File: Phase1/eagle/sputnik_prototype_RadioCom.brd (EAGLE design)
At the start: 99 x 100 mm, 103 parts, among them Y1 32MHz

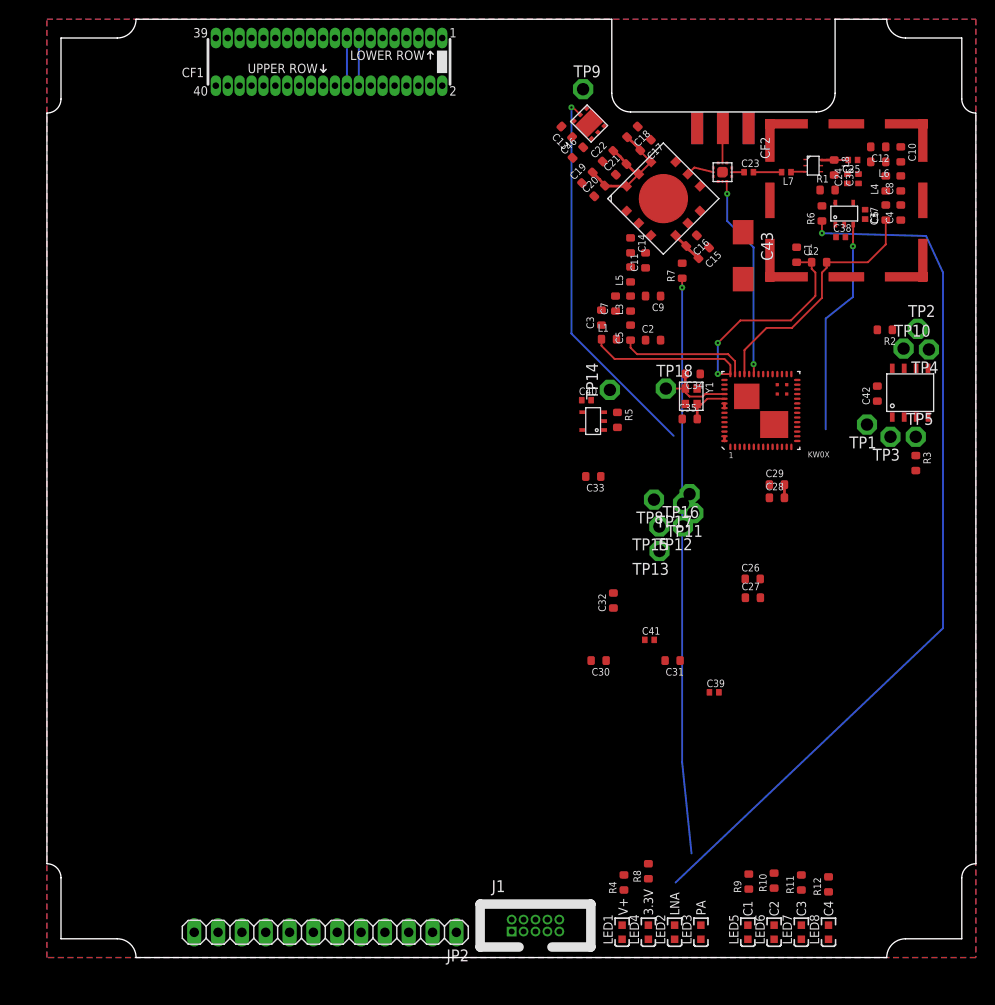
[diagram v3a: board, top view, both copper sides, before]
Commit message: Yep, that was a good idea. I added the other shield. And experimented with other layouts. Still needs a ton of work, but now it's going to be OK. OH CRAP the RXTX switch might have be wired the otherway: check this. That said, I think this is more sane. Power and nd caps need to be laid out, then signals.
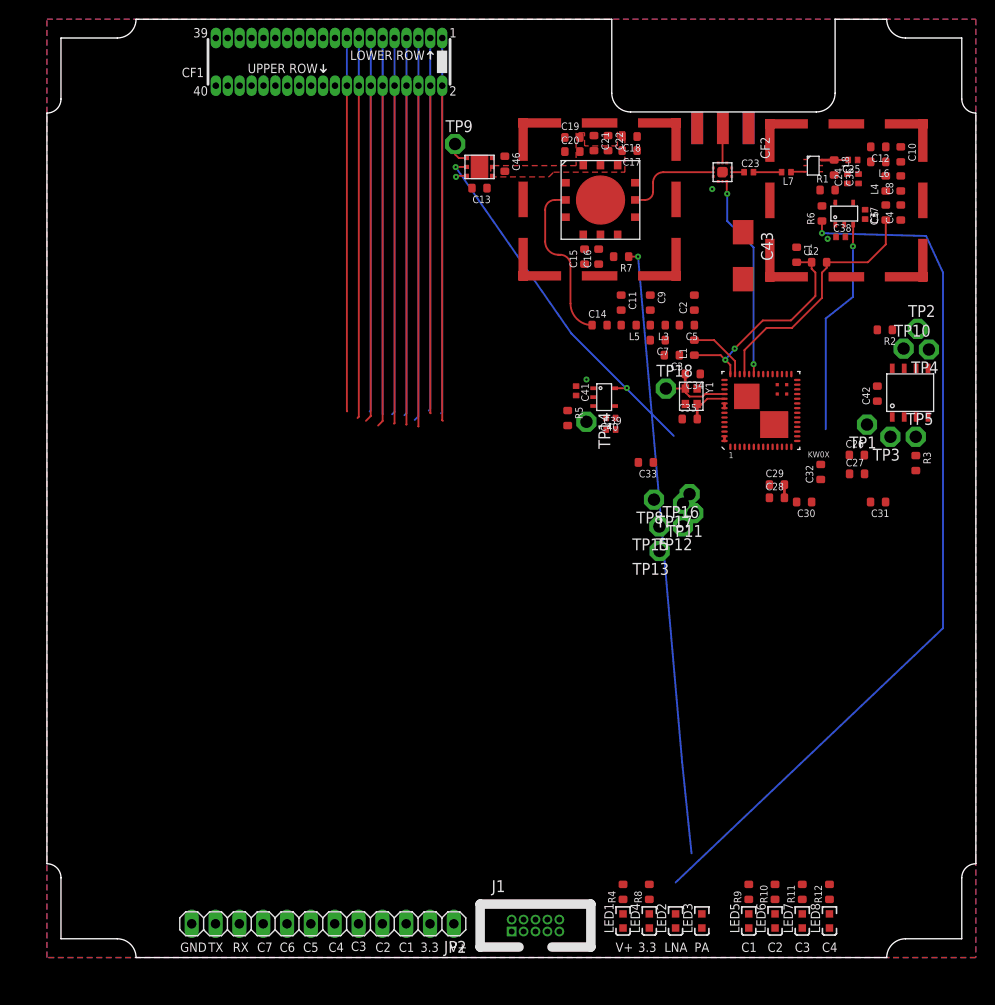
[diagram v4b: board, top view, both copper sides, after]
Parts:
- added SH2: BMI-S-202-SHIELD, hw-laird-bmi-s-202:BMI-S-202
- moved C39 30.1 mm to (60.1, 56.3)
- moved C41 27.7 mm to (56.4, 60.4), turned to 270 degrees
- moved C30 27.7 mm to (80.7, 48.5)
- moved C31 27.7 mm to (88.6, 48.5)
- moved C32 26.0 mm to (82.5, 51.8)
- moved C27 17.2 mm to (86.3, 51.5)
- moved C26 17.2 mm to (86.3, 53.5)
- moved TP9 14.8 mm to (43.5, 86.7)
- moved U$9 12.8 mm to (44.6, 83.0), turned to 90 degrees
- moved C15 12.7 mm to (57.3, 74.7), turned to 90 degrees
- moved C13 11.1 mm to (46.1, 82.0), turned to 180 degrees
- moved C16 10.0 mm to (58.8, 74.7), turned to 90 degrees
- moved L1 9.14 mm to (69.0, 65.0), turned to 90 degrees
- moved C14 9.12 mm to (58.9, 67.4), turned to 0 degrees
- moved C3 8.50 mm to (66.6, 64.2), turned to 180 degrees
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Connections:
- net V+ renamed RIP
- net GND: now also SH2.P$1, SH2.P$10, SH2.P$11, SH2.P$12, SH2.P$2, SH2.P$3, SH2.P$4, SH2.P$5, SH2.P$6, SH2.P$7, SH2.P$8, SH2.P$9
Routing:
- net PTC3: track 0.00 -> 40.9 mm
- net PTC5: track 0.00 -> 40.3 mm
- net PTC7: track 0.00 -> 40.2 mm
- net PTE16: track 0.00 -> 40.1 mm
- net PTB2: track 0.00 -> 40.1 mm
- net PTE18: track 0.00 -> 39.8 mm
- net PTC1: track 0.00 -> 39.8 mm
- net PTE17: track 0.00 -> 36.4 mm
- net PTC4: track 0.00 -> 36.3 mm
- net PTC6: track 0.00 -> 36.1 mm
- net PTD0: track 0.00 -> 36.0 mm
- net PTE19: track 0.00 -> 35.9 mm
- net PTB17: track 0.00 -> 35.7 mm
- net UART0_TX: track 5.08 -> 40.6 mm
- net PTC2: track 0.00 -> 34.9 mm
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- added copper zone on layer 15, net 3.3V
- added copper zone on layer 15, net RIP
- added copper zone on layer 1, net VPA
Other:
- board text added: "3.3"
- board text added: "C5"
- board text added: "C6"
- board text added: "C7"
- board text added: "GND"
- board text added: "RX"
- board text added: "TX"
- board text removed: "3.3V"

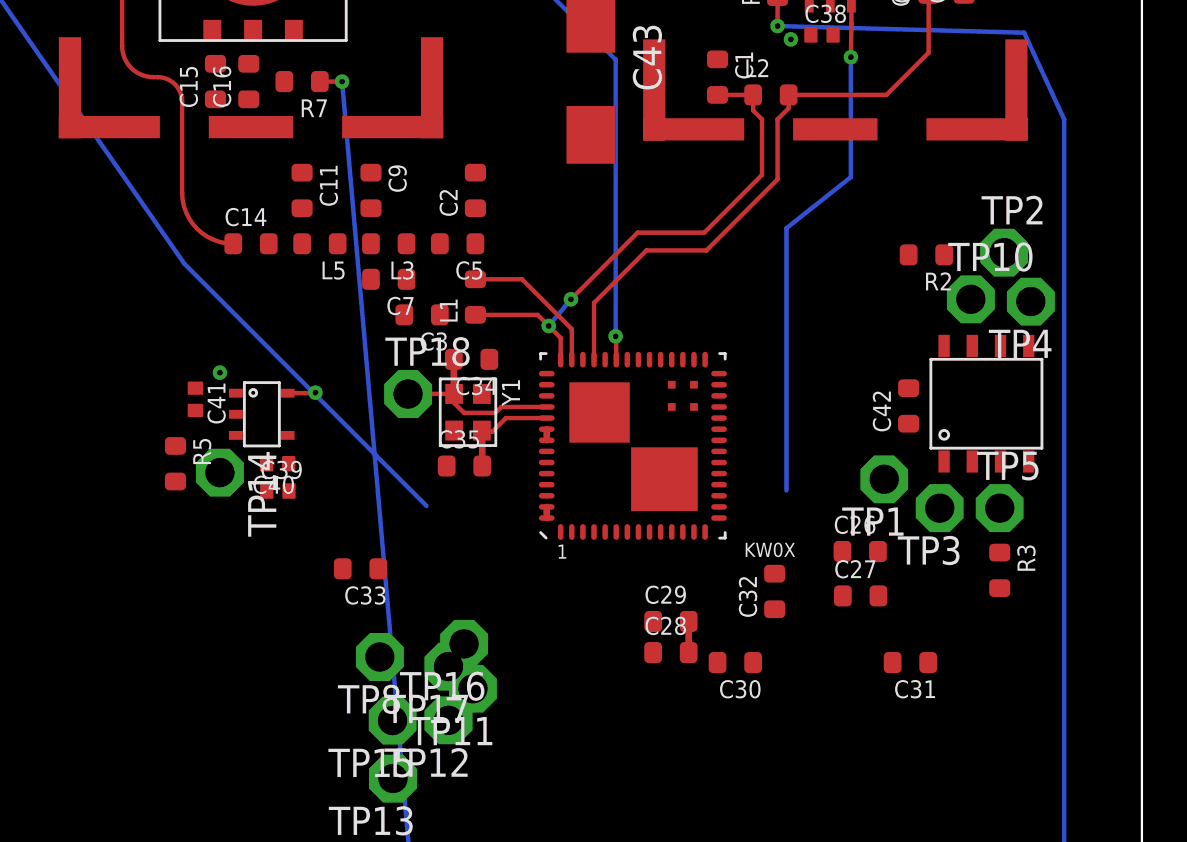
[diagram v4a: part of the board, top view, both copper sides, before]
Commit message: Attached bypass caps, made some connections between LDO and SPI cache components
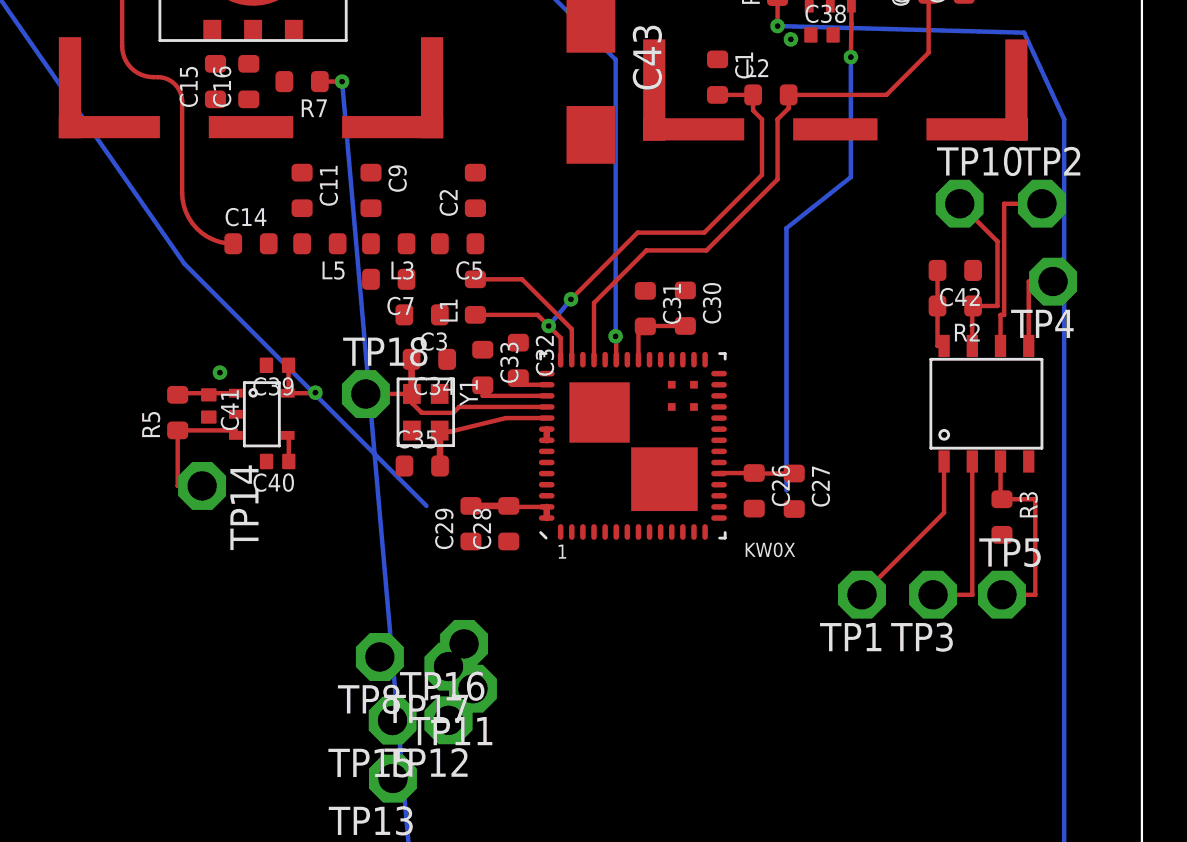
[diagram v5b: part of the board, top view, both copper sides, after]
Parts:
- moved C31 19.9 mm to (76.7, 64.5), turned to 270 degrees
- moved C30 16.1 mm to (78.5, 64.5), turned to 270 degrees
- moved C32 15.5 mm to (70.9, 62.1), turned to 270 degrees
- moved C33 10.6 mm to (69.3, 61.8), turned to 270 degrees
- moved C29 10.0 mm to (68.8, 54.8), turned to 90 degrees
- moved C28 9.32 mm to (70.5, 54.8), turned to 90 degrees
- moved C42 6.45 mm to (90.6, 66.2), turned to 180 degrees
- moved C39 5.66 mm to (60.1, 61.9), turned to 180 degrees
- moved C27 5.58 mm to (83.3, 56.3), turned to 270 degrees
- moved C26 5.50 mm to (81.5, 56.3), turned to 270 degrees
- moved TP1 5.30 mm to (86.4, 51.6)
- moved TP10 4.33 mm to (90.8, 69.2)
- moved TP3 3.91 mm to (89.6, 51.6)
- moved TP5 3.90 mm to (92.7, 51.6)
- moved TP2 2.78 mm to (94.5, 69.2)
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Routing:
- net 3.3V: track 3.16 -> 17.3 mm
- net N$11: track 0.00 -> 9.06 mm
- net SCLK: track 0.00 -> 8.27 mm
- net !HOLD: track 0.00 -> 8.24 mm
- net MISO: track 0.00 -> 7.77 mm
- net !CS: track 0.00 -> 7.53 mm
- net N$12: track 0.00 -> 6.45 mm
- net MOSI: track 0.00 -> 4.00 mm
- net N$34: track 0.00 -> 3.36 mm
- net RIP: track 1.32 -> 4.09 mm
- net N$6: track 8.50 -> 10.4 mm
- net N$8: track 4.80 -> 6.52 mm
- net N$31: track 0.00 -> 1.58 mm
- net N$13: track 0.00 -> 1.23 mm

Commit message: Fixed symbol pins and locations
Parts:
- removed L7: (no value), rcl_custom:.0402-B-NOSILK
- added C44: 10nF, rcl_custom:.0402-B-NOSILK
- C24: value 10nF -> 1nF
- L8: value 150nH -> 82nH
- moved PA 5.80 mm to (58.9, 80.8)
- moved U$1 3.61 mm to (92.0, 59.6)
- moved U$7 1.68 mm to (84.8, 79.0)
- moved TRSWITCH 1.41 mm to (72.0, 83.7)
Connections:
- removed net N$24: L7.1, LNA.3
- net GND: now also C44.2
- net LNA_IN: now also TRSWITCH.8; no longer TRSWITCH.2
- net N$2: now also TRSWITCH.2; no longer TRSWITCH.8
- net N$25: now also LNA.3; no longer L7.2
- net VBIAS: now also C44.1
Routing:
- net 3.3V: track 17.3 -> 20.6 mm
- net N$25: track 3.00 -> 0.00 mm
- net N$2: track 10.1 -> 12.3 mm
- net LNA_IN: track 1.32 -> 3.26 mm
- net N$12: track 6.45 -> 8.13 mm
- net N$13: track 1.23 -> 2.90 mm
- net N$24: track 1.58 -> 0.00 mm
- net RIP: track 4.09 -> 4.80 mm
- net N$4: track 2.50 -> 3.09 mm
- net SCLK: track 8.27 -> 8.83 mm
- net !HOLD: track 8.24 -> 8.81 mm
- net MOSI: track 4.00 -> 4.56 mm
- net MISO: track 7.77 -> 7.20 mm
- net !CS: track 7.53 -> 6.96 mm
- net N$11: track 9.06 -> 8.50 mm

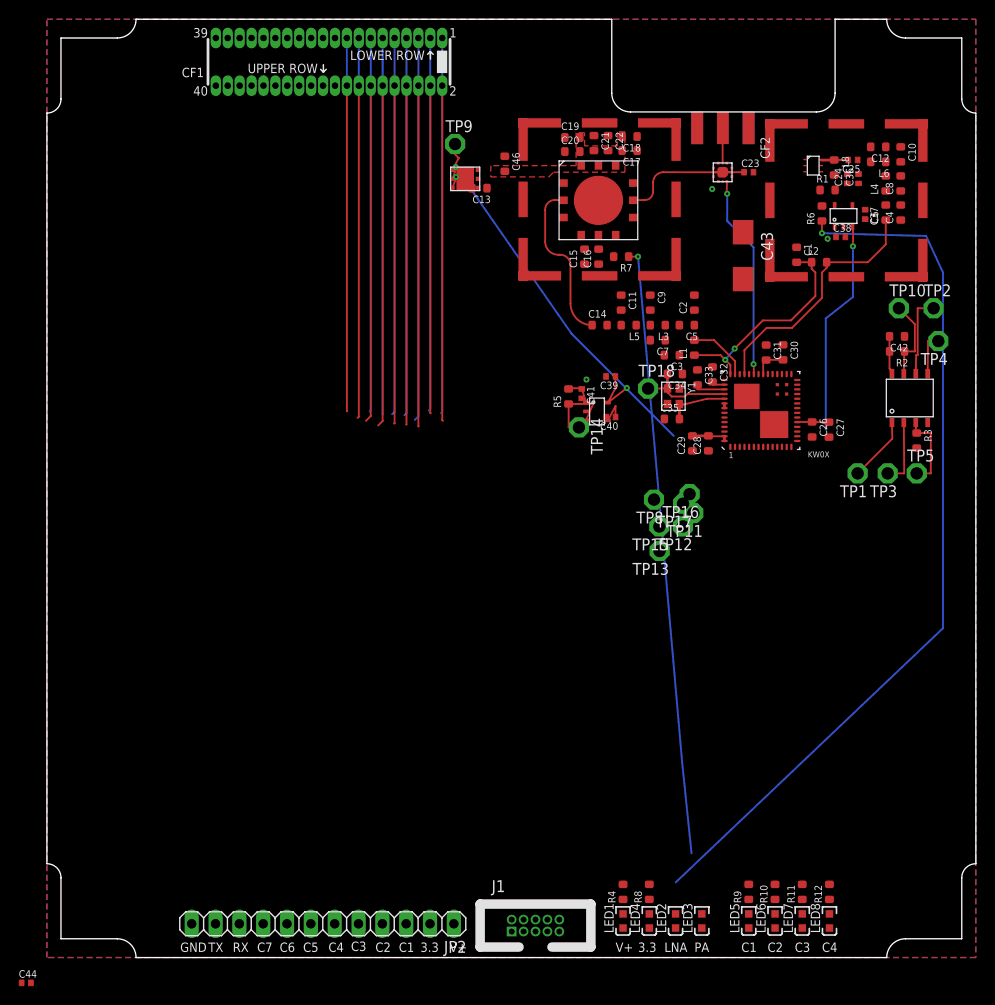
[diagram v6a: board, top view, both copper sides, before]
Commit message: Added RIP and 3.3V lines
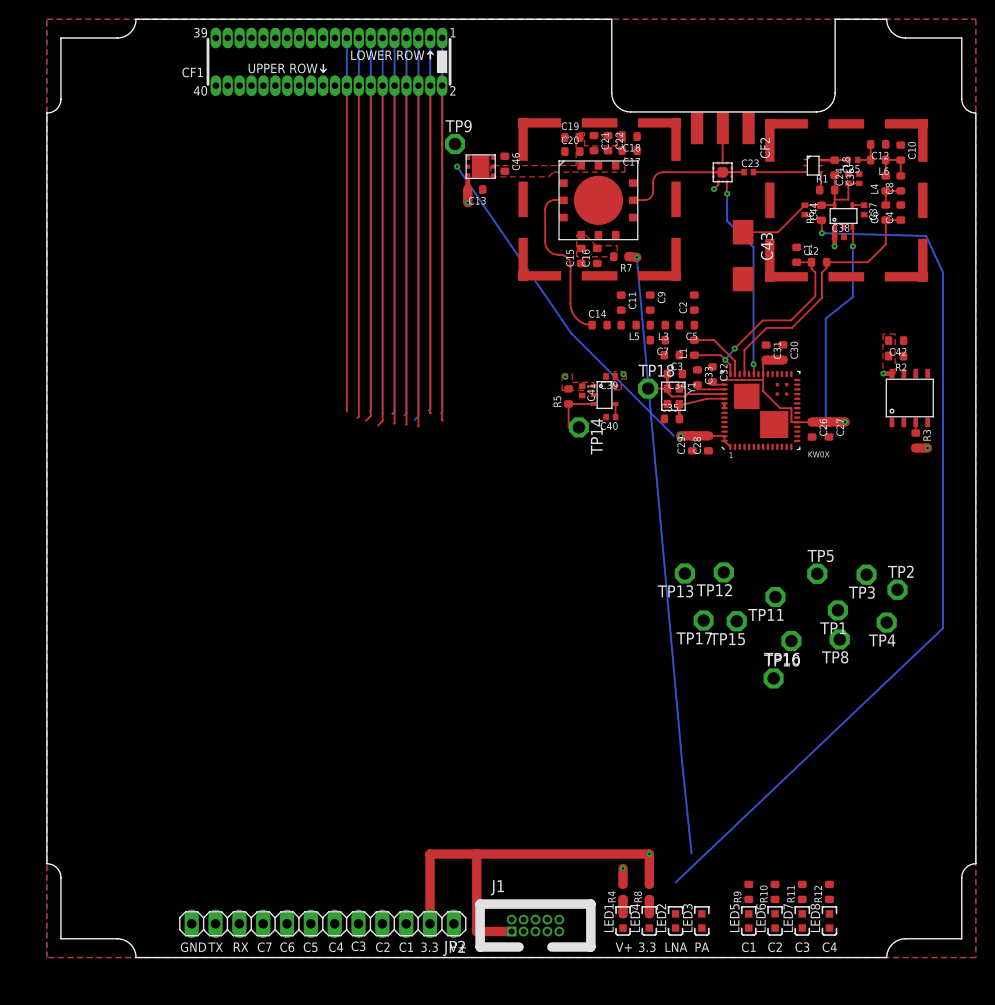
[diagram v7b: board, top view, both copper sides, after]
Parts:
- moved C44 116.9 mm to (80.8, 79.7), turned to 270 degrees
- moved TP10 41.6 mm to (77.5, 29.8)
- moved TP4 30.5 mm to (89.5, 35.7)
- moved TP2 30.2 mm to (90.7, 39.2)
- moved TP8 24.8 mm to (84.5, 33.9)
- moved TP16 19.0 mm to (79.3, 33.7)
- moved TP5 15.1 mm to (82.1, 40.9)
- moved TP1 14.8 mm to (84.3, 37.0)
- moved TP15 13.0 mm to (73.5, 35.8)
- moved TP17 12.6 mm to (70.0, 35.9)
- moved TP11 12.5 mm to (77.6, 38.4)
- moved TP3 11.0 mm to (87.3, 40.8)
- moved TP12 6.55 mm to (72.1, 41.0)
- moved TP13 3.61 mm to (68.0, 40.9)
- moved U$9 2.10 mm to (46.2, 84.3)
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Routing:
- net 3.3V: track 20.6 -> 110.9 mm, vias 1 -> 6
- net RIP: track 4.80 -> 83.7 mm, vias 4 -> 5
- net VBIAS: track 0.21 -> 18.5 mm
- net SCLK: track 8.83 -> 0.00 mm
- net !HOLD: track 8.81 -> 0.00 mm
- net N$11: track 8.50 -> 1.15 mm
- net MISO: track 7.20 -> 0.00 mm
- net !CS: track 6.96 -> 0.00 mm
- net N$25: track 0.00 -> 5.58 mm
- net N$19: track 0.00 -> 5.02 mm
- net MOSI: track 4.56 -> 0.00 mm
- net N$18: track 0.00 -> 3.10 mm
- net N$4: track 3.09 -> 0.00 mm
- net LNA_OUT: track 0.00 -> 3.05 mm
- net N$27: track 0.00 -> 2.09 mm
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- added copper zone on layer 1, net 3.3V
- added copper zone on layer 1, net RIP

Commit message: Started working on GPIOs. Finished V_LNA and VPA lines
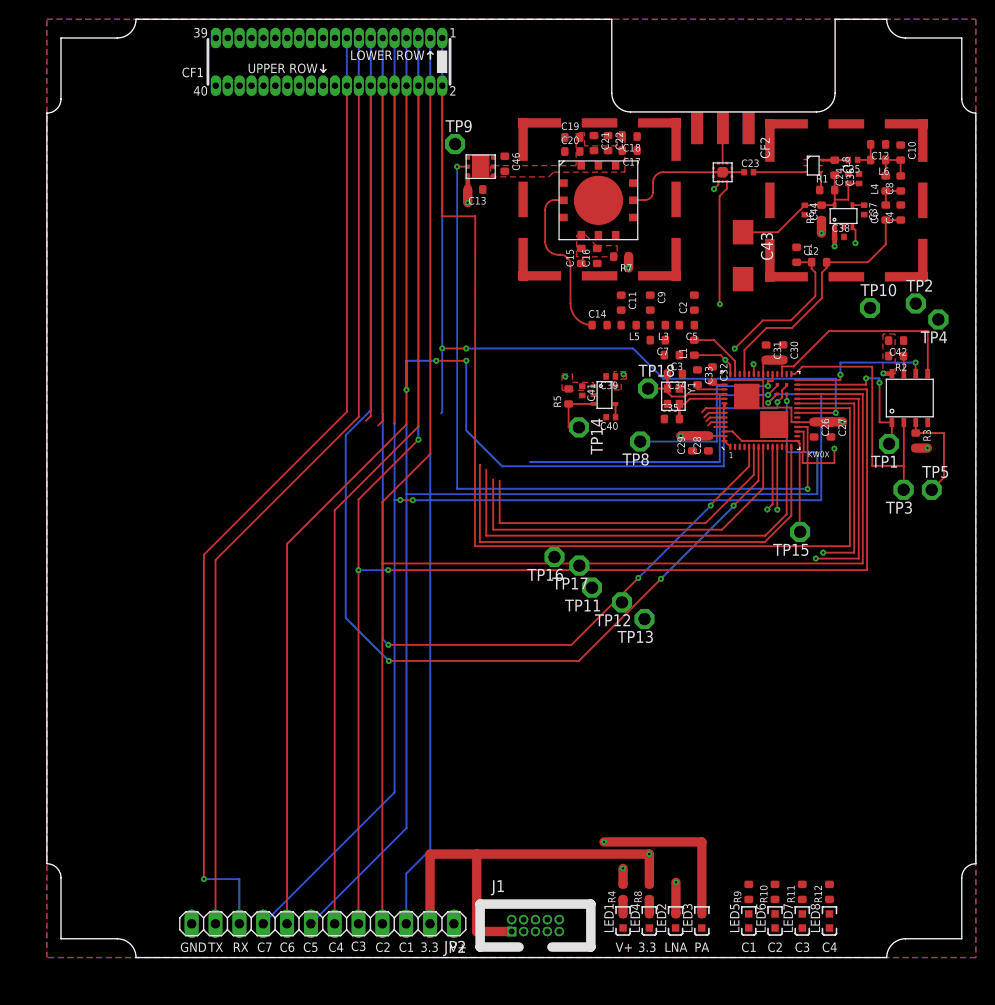
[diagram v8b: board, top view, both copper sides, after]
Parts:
- moved TP10 40.8 mm to (87.7, 69.2)
- moved TP4 32.8 mm to (95.0, 68.0)
- moved TP2 30.6 mm to (92.6, 69.7)
- moved TP8 30.0 mm to (63.2, 55.0)
- moved TP16 26.8 mm to (54.1, 42.7)
- moved TP11 19.6 mm to (58.1, 39.4)
- moved TP1 18.6 mm to (89.8, 54.8)
- moved TP5 15.1 mm to (94.3, 49.9)
- moved TP17 14.5 mm to (56.7, 41.8)
- moved TP15 11.7 mm to (80.3, 45.4)
- moved TP12 11.3 mm to (61.3, 37.9)
- moved TP3 9.87 mm to (91.3, 49.9)
- moved TP13 6.48 mm to (63.7, 36.1)
- moved C26 0.21 mm to (81.8, 56.3)
- moved C27 0.21 mm to (83.6, 56.3)
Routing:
- net PTC3: track 40.9 -> 177.9 mm, vias 0 -> 3
- net PTC2: track 34.9 -> 167.7 mm
- net PTC7: track 40.2 -> 164.5 mm, vias 0 -> 3
- net PTC6: track 36.1 -> 155.4 mm, vias 0 -> 4
- net PTC5: track 40.3 -> 156.3 mm, vias 0 -> 1
- net UART0_RX: track 39.8 -> 154.4 mm, vias 0 -> 1
- net UART0_TX: track 40.6 -> 147.9 mm
- net PTC1: track 39.8 -> 123.6 mm, vias 0 -> 1
- net PTC4: track 36.3 -> 118.3 mm, vias 0 -> 1
- net PTE18: track 39.8 -> 120.4 mm, vias 0 -> 3
- net PTB17: track 35.7 -> 112.9 mm
- net PTE16: track 40.1 -> 113.4 mm, vias 0 -> 3
- net PTB2: track 40.1 -> 91.1 mm, vias 0 -> 3
- net PA_EN: track 37.0 -> 80.6 mm, vias 1 -> 2
- net PTE19: track 35.9 -> 76.3 mm
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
